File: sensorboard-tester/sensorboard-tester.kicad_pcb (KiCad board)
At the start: 2 copper layers, 83.8 x 83.8 mm, 38 parts, among them J0 Power, J1 USB_B, J2 LEDCurrentProbe, J3 Sensor, J4 PTVoltage, J5 StabilizingCap, J6 PTCurrent, J7 Sensor, J8 PTVoltage, J9 PTCurrent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

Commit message: Include mirrored headers for the sensorboards, in case their header has to be flipped.
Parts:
- added J10: MirrorSensor, Pin_Headers:Pin_Header_Straight_2x02_Pitch2.54mm, F.Cu at (70.5, 109.5)
- added J11: Sensor, Pin_Headers:Pin_Header_Straight_2x02_Pitch2.54mm, F.Cu at (113.0, 109.5)
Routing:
- net /Cathode: track 208.1 -> 201.3 mm, vias 0 -> 1
- net /Anode: track 184.6 -> 178.1 mm, vias 0 -> 1
- net +3V3: track 46.4 -> 52.8 mm
- net /Simple/Emitter: track 43.5 -> 49.5 mm
- net /Simple/Collector: track 75.7 -> 81.8 mm
- net /Transimpedance/Emitter: track 46.7 -> 51.7 mm
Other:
- board text added: "Back"
- board text added: "Front"

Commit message: Add/update board rev silkscreen, nothing else
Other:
- board text added: "http://github.com/jkominek/piano-conversion Sensorboard tester Rev0"

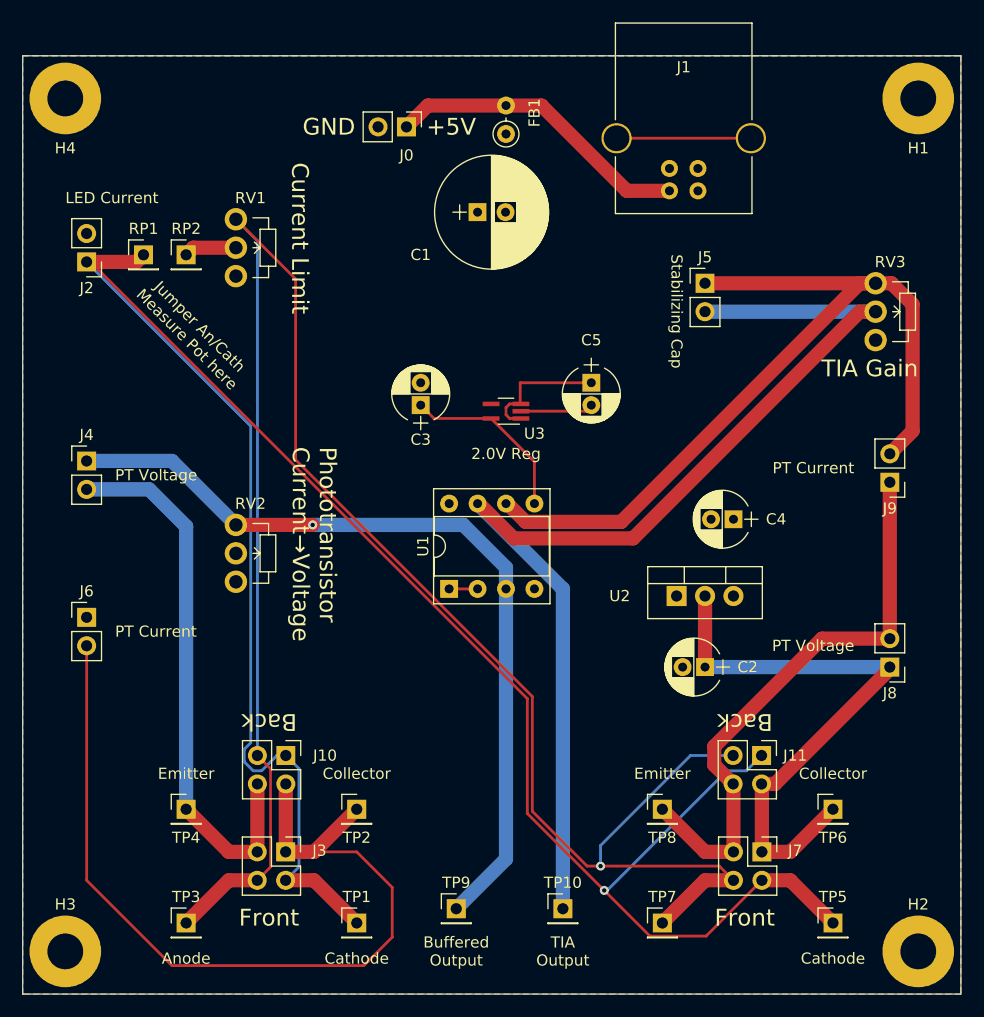
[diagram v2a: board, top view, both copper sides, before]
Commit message: Cleanup and reconcile the headers. Switch to SOT23 regulators for both.
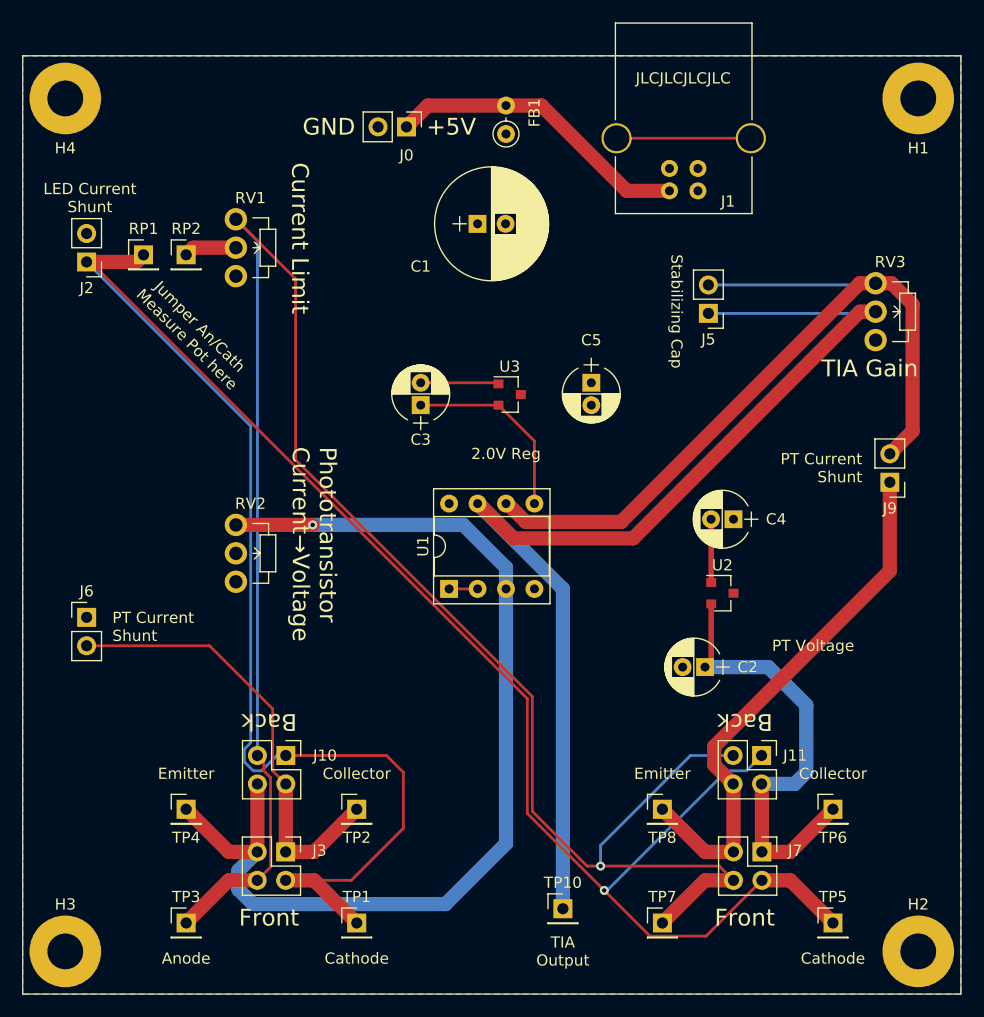
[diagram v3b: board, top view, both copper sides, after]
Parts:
- removed J4, J8: PTVoltage, Pin_Headers:Pin_Header_Straight_1x02_Pitch2.54mm
- removed TP9: BufferedOut, Pin_Headers:Pin_Header_Straight_1x01_Pitch2.54mm
- J2: value LEDCurrentProbe -> LEDCurrentShunt
- J6, J9: value PTCurrent -> PTCurrentShunt
- U2: value LD1086V33-DG -> AP2120N-3.3TRG1; footprint TO_SOT_Packages_THT:TO-220-3_Vertical -> TO_SOT_Packages_SMD:SOT-23
- U3: value MIC5366-2.0YC5-TR -> MCP1700T-2002E/TT; footprint TO_SOT_Packages_SMD:SOT-353_SC-70-5_Handsoldering -> TO_SOT_Packages_SMD:SOT-23
- moved U2 4.10 mm to (109.5, 95.0)
- moved J5 2.71 mm to (108.2, 70.0), turned to 180 degrees
- moved U3 1.53 mm to (90.5, 77.2), turned to 0 degrees
- moved C1 1.04 mm to (87.6, 62.0)
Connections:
- J10 pad 4: /Simple/Emitter -> /Simple/OP+
- J3 pad 3: /Simple/Emitter -> /Simple/OP+
- J5 pad 1: /Transimpedance/OP- -> /Transimpedance/OP_OUT
- J5 pad 2: /Transimpedance/OP_OUT -> /Transimpedance/OP-
- TP4 pad 1: /Simple/Emitter -> /Simple/OP+
- U3 pad 1: +5V -> GND
- U3 pad 2: GND -> /Transimpedance/OP+
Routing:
- net /Simple/Emitter: track 49.5 -> 0.00 mm
- net /Simple/Collector: track 81.8 -> 40.2 mm
- net /Simple/OP+: track 73.7 -> 95.1 mm
- net /Cathode: track 201.3 -> 215.2 mm
- net +3V3: track 52.8 -> 40.8 mm
- net +5V: track 16.5 -> 4.71 mm
- net GND: track 6.51 -> 12.7 mm
- net /Transimpedance/Emitter: track 51.7 -> 48.2 mm
- net /Transimpedance/OP+: track 16.0 -> 17.1 mm
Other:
- board text added: "JLCJLCJLCJLC"
- board text added: "LED Current Shunt"
- board text added: "PT Current Shunt"
- board text added: "http://github.com/jkominek/piano-conversion Sensorboard tester Rev1"
- board text removed: "Buffered Output"
- board text removed: "LED Current"
- board text removed: "PT Current"
- board text removed: "http://github.com/jkominek/piano-conversion Sensorboard tester Rev0"
